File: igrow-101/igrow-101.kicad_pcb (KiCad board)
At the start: 2 copper layers, 49.8 x 39.5 mm, 30 parts, among them P1 CONN_02X05, Q1 NPN, Q2 NPN, Q3 NPN, SW1 SW_PUSH, U1 NRF51822-MODULE, U2 SHT21, U3 TL972

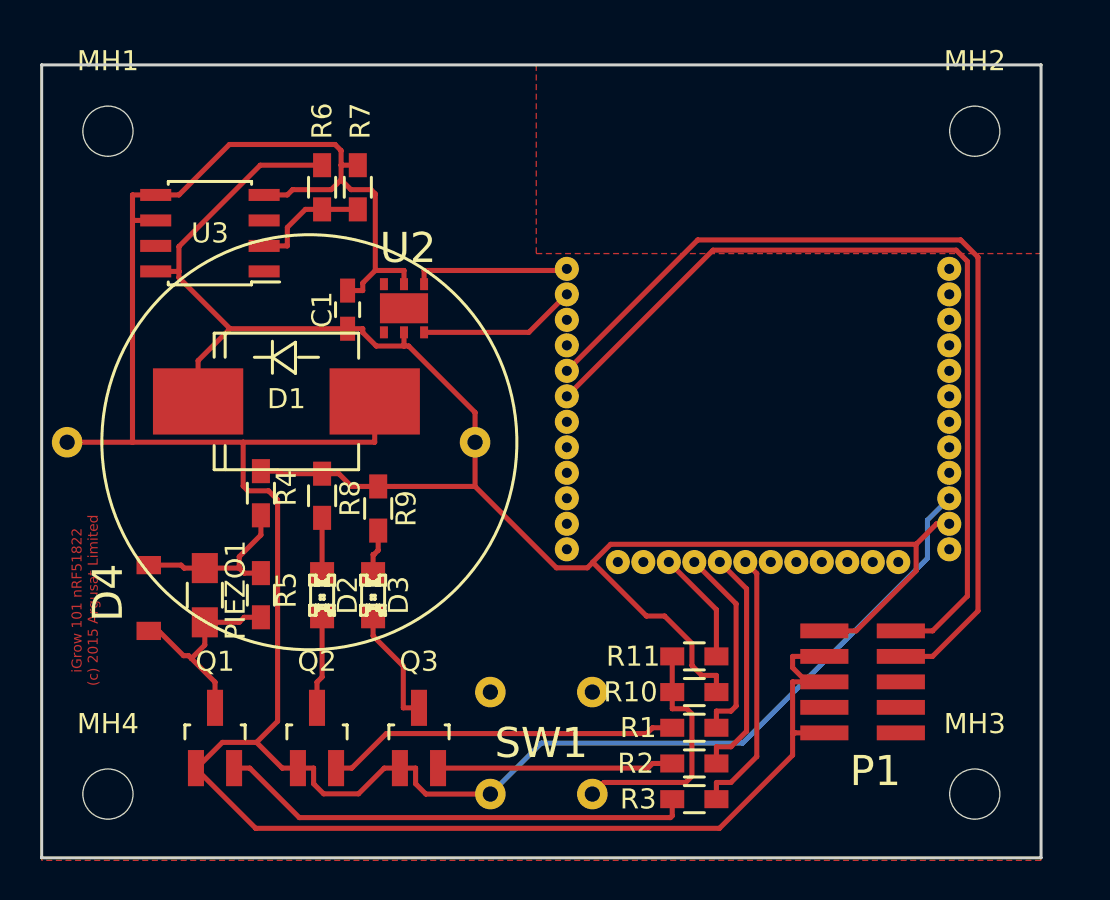
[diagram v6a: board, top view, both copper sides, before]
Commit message: Rework with 0.381mm minimum track widths
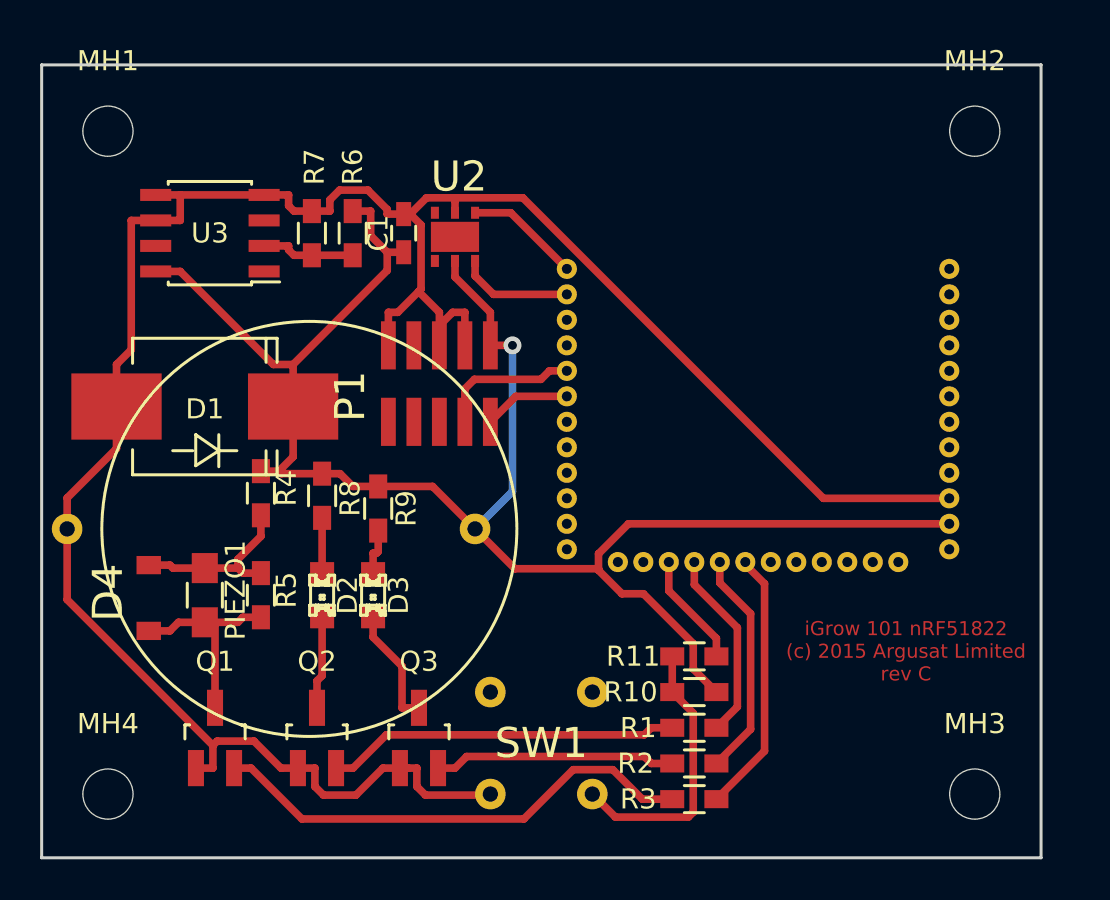
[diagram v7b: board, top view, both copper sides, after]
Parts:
- moved P1 21.9 mm to (153.7, 107.2), turned to 270 degrees
- moved C1 4.72 mm to (149.4, 101.6)
- moved U2 4.37 mm to (152.9, 100.6)
- moved BT1 4.32 mm to (152.9, 116.3)
- moved D1 4.07 mm to (139.4, 110.2), turned to 0 degrees
- moved R7 3.23 mm to (144.8, 101.6)
- moved R6 2.75 mm to (146.8, 101.6)
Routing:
- net GND: track 166.3 -> 116.4 mm
- net Net-(P1-Pad2): track 43.9 -> 4.34 mm
- net Net-(P1-Pad4): track 45.9 -> 7.10 mm
- net VCC: track 92.1 -> 88.8 mm, vias 0 -> 1
- net Net-(U1-Pad35): track 7.90 -> 5.70 mm
- net Net-(U1-Pad36): track 7.83 -> 5.73 mm
- net Net-(R10-Pad2): track 12.1 -> 13.8 mm
- net Net-(R6-Pad2): track 5.96 -> 4.72 mm
- net Net-(Q1-Pad2): track 23.7 -> 24.5 mm
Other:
- net class Default: trace_width 0.327 -> 0.381
- rule trace_min: 0.327 -> 0.254
- board text added: "iGrow 101 nRF51822 (c) 2015 Argusat Limited rev C"
- board text removed: "iGrow 101 nRF51822 (c) 2015 Argusat Limited"

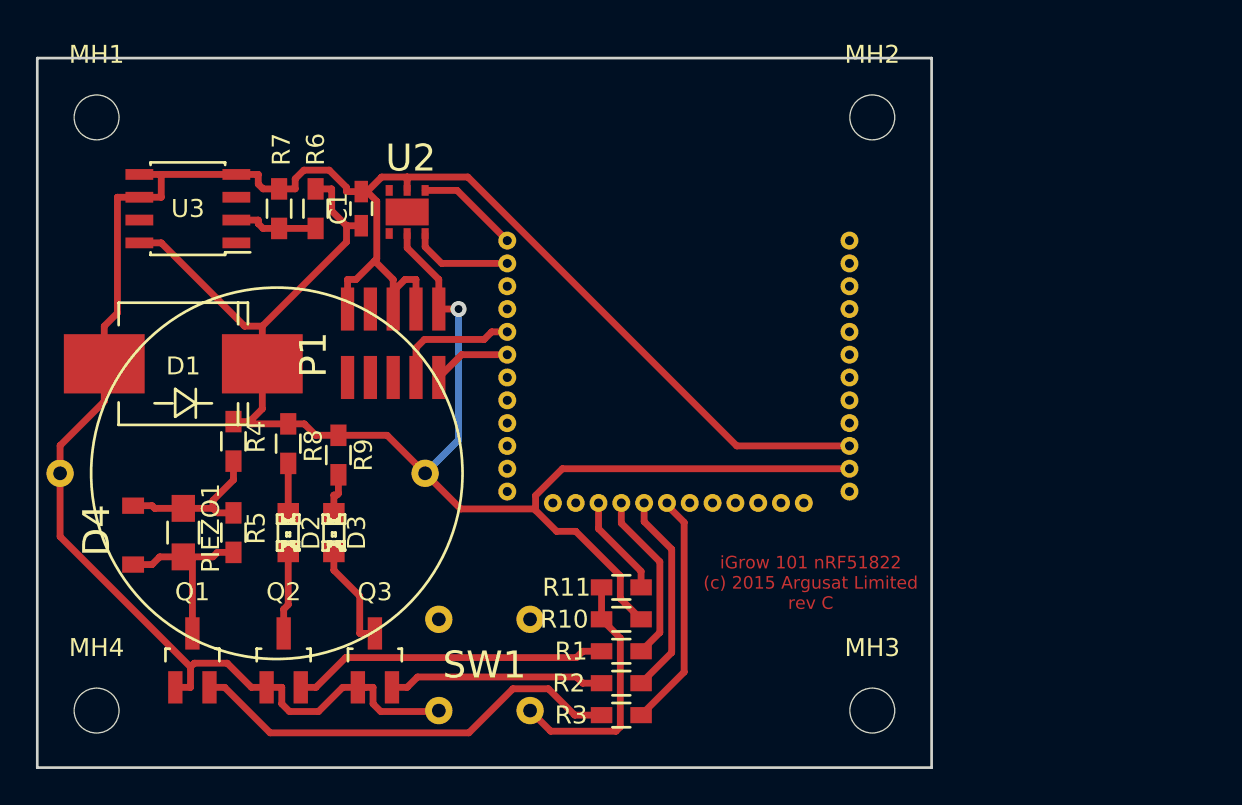
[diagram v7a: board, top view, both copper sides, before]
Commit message: Rework with 0.508mm/20mil minimum track widths
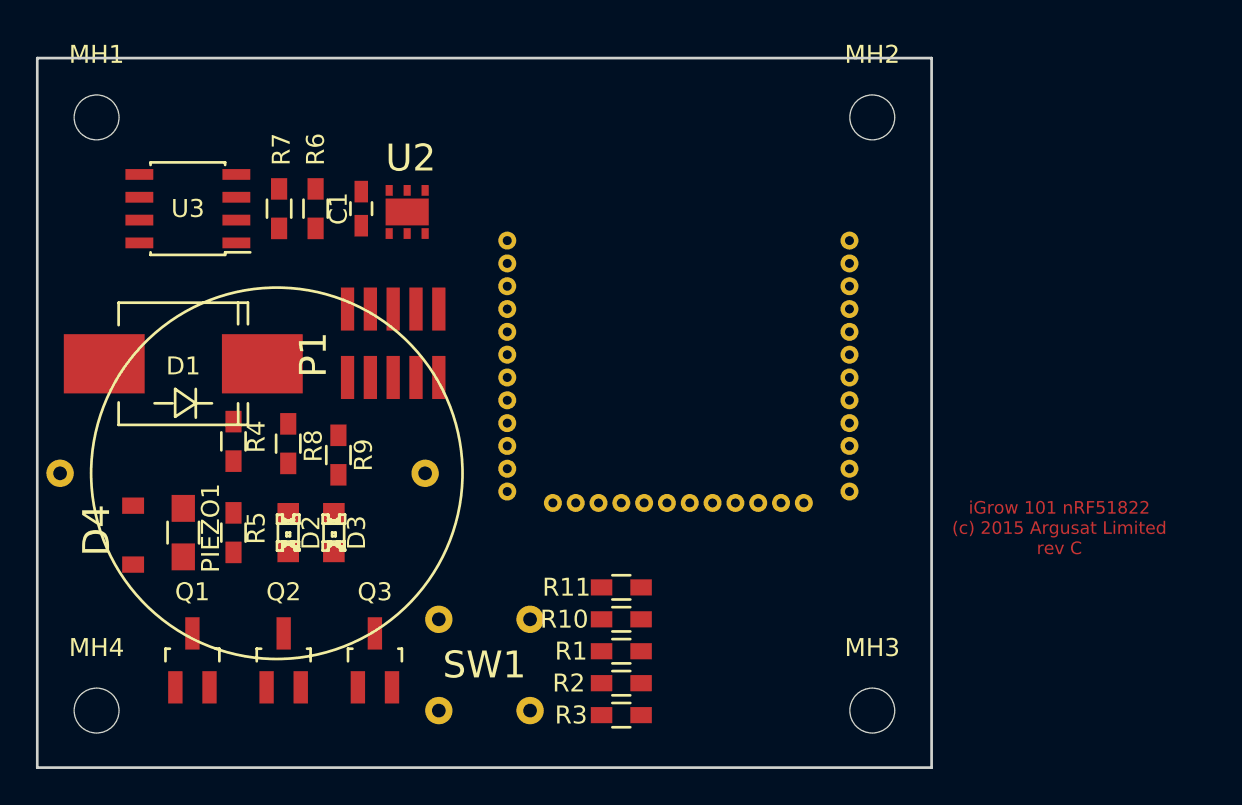
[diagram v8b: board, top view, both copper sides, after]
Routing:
- net GND: track 116.4 -> 0.00 mm
- net VCC: track 88.8 -> 0.00 mm, vias 1 -> 0
- net Net-(Q1-Pad2): track 24.5 -> 0.00 mm
- net Net-(Q2-Pad2): track 17.6 -> 0.00 mm
- net Net-(R10-Pad2): track 13.8 -> 0.00 mm
- net Net-(R3-Pad2): track 13.2 -> 0.00 mm
- net Net-(Q3-Pad2): track 12.0 -> 0.00 mm
- net Net-(R2-Pad2): track 11.4 -> 0.00 mm
- net Net-(D4-Pad1): track 10.1 -> 0.00 mm
- net Net-(R1-Pad2): track 9.58 -> 0.00 mm
- net Net-(D4-Pad2): track 8.86 -> 0.00 mm
- net Net-(P1-Pad4): track 7.10 -> 0.00 mm
- net Net-(D3-Pad2): track 6.00 -> 0.00 mm
- net Net-(U1-Pad36): track 5.73 -> 0.00 mm
- net Net-(U1-Pad35): track 5.70 -> 0.00 mm
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- removed copper zone on F.Cu, net GND
